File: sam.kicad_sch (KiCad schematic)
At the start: 46 parts, among them IC1 4164, IC15 MC6883, IC16 74LS244N, IC2 4164, IC3 4164, IC31 74LS02N, IC33 74AHCT138N, IC36 74LS132, IC37 GAL, IC4 4164, IC5 4164, IC6 4164, IC7 4164, IC8 4164, U1 74HCT138

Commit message: move to samx4
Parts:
- removed C11, C37: 4.7uF, Capacitor_THT:CP_Radial_D5.0mm_P2.50mm, symbol Device:C_Polarized_Small
- removed C14, C15, C16, C17, C18, C19, C20, C21: 0.1uF, Capacitor_THT:C_Disc_D4.3mm_W1.9mm_P5.00mm, symbol Device:C_Small
- removed C40: 22pF, Capacitor_THT:C_Disc_D3.0mm_W2.0mm_P2.50mm, symbol Device:C_Small
- removed C41: 33pF, Capacitor_THT:C_Disc_D3.0mm_W2.0mm_P2.50mm, symbol Device:C_Small
- removed IC1, IC2, IC3, IC4, IC5, IC6, IC7, IC8: 4164, Package_DIP:DIP-16_W7.62mm, symbol Memory_RAM_Siemens:HYB4116
- removed IC15: MC6883, Package_DIP:DIP-40_W15.24mm, symbol Memory_Controller_Motorola:MC6883
- removed unit 2 of IC36
- removed unit 4 of IC36
- removed unit 3 of IC36
- removed unit 1 of IC36
- removed IC37: GAL, Package_DIP:DIP-24_W7.62mm, symbol vdg:GAL22V10
- removed JP5: Z8hi/low, Jumper:SolderJumper-3_P1.3mm_Open_Pad1.0x1.5mm, symbol Jumper:Jumper_3_Bridged12
- removed R12, R20, R21, R22, R23, R24, R25, R26, R27, R28, R66: 22R, Resistor_THT:R_Axial_DIN0207_L6.3mm_D2.5mm_P2.54mm_Vertical, symbol Device:R_Small
- removed R37: 1K5, Resistor_THT:R_Axial_DIN0207_L6.3mm_D2.5mm_P10.16mm_Horizontal, symbol Device:R_Small
- removed XL2: 14.31818MHz, Crystal:Crystal_HC49-U_Horizontal, symbol Device:Crystal_Small
- added C11, C13, C14, C15, C16, C7: 100n, Capacitor_SMD:C_0603_1608Metric, symbol Device:C
- added C3, C5: 0.1uF, Capacitor_THT:C_Disc_D4.3mm_W1.9mm_P5.00mm, symbol Device:C_Small
- added C6: 4.7uF, Capacitor_THT:CP_Radial_D5.0mm_P2.50mm, symbol Device:C_Polarized_Small
- added C8: 1u, Capacitor_SMD:C_0805_2012Metric, symbol Device:C
- added C9: 2u2, Capacitor_SMD:C_0603_1608Metric, symbol Device:C
- added IC11: 74LS244N, Package_DIP:DIP-20_W7.62mm, symbol 74xx:74LS244
- added J4: JTAG, Connector_PinHeader_2.54mm:PinHeader_1x06_P2.54mm_Vertical, symbol Connector_Generic:Conn_01x06
- added R10, R11, R17, R18, R2, R3, R4, R6, R7, R8, R9: 22R, Resistor_THT:R_Axial_DIN0207_L6.3mm_D2.5mm_P2.54mm_Vertical, symbol Device:R_Small
- added R5: 100R, Resistor_THT:R_Axial_DIN0207_L6.3mm_D2.5mm_P2.54mm_Vertical, symbol Device:R_Small
- added U1, U2: ~, symbol Motorola PIA:AS6C1008
- added U3: XC95144XL-TQ100, Package_QFP:TQFP-100_14x14mm_P0.5mm, symbol CPLD_Xilinx:XC95144XL-TQ100
- added U4: TPS7A2433DBVR, Package_TO_SOT_SMD:SOT-23-5, symbol Regulator_Linear:TPS7A0533PDBV
- added X1: 14.31818MHz, Oscillator:Oscillator_SMD_ECS_2520MV-xxx-xx-4Pin_2.5x2.0mm, symbol Oscillator:ECS-2520MV-xxx-xx
- C12: footprint Capacitor_THT:C_Rect_L7.0mm_W2.5mm_P5.00mm -> Capacitor_SMD:C_0603_1608Metric; JLCPCB BOM (none) -> 0; LCSC Part (none) -> C149620
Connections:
- net +5V: now also C3.2, C5.2, C6.1, C8.1, IC11.20 (VCC), U1.6 (CE2), U1.8 (Vcc), U2.8 (Vcc), U4.1 (IN), U4.3 (EN); no longer C12.1
- net A0: now also U1.20 (A0), U2.20 (A0), U3.80 (P80)
- net A1: now also U1.19 (A1), U2.19 (A1), U3.78 (P78)
- net A10: now also U1.31 (A10), U2.31 (A10), U3.19 (P19)
- net A11: now also U1.1 (A11), U2.1 (A11), U3.20 (P20)
- net A12: now also U1.12 (A12), U2.12 (A12), U3.12 (P12)
- net A13: now also U1.4 (A13), U2.4 (A13), U3.14 (P14)
- net A14: now also U1.11 (A14), U2.11 (A14), U3.9 (P9)
- net A15: now also U1.7 (A15), U2.7 (A15), U3.8 (P8)
- net A2: now also U1.18 (A2), U2.18 (A2), U3.76 (P76)
- net A3: now also U1.17 (A3), U2.17 (A3), U3.63 (P63)
- net A4: now also U1.16 (A4), U2.16 (A4), U3.58 (P58)
- net A5: now also U1.15 (A5), U2.15 (A5), U3.59 (P59)
- net A6: now also U1.14 (A6), U2.14 (A6), U3.60 (P60)
- net A7: now also U1.13 (A7), U2.13 (A7), U3.61 (P61)
- net A8: now also U1.3 (A8), U2.3 (A8), U3.17 (P17)
- net A9: now also U1.2 (A9), U2.2 (A9), U3.18 (P18)
- net D0: now also IC11.15 (I2b)
- net D1: now also IC11.13 (I1b)
- net D2: now also IC11.4 (I1a)
- net D3: now also IC11.2 (I0a)
- net D4: now also IC11.17 (I3b)
- net D5: now also IC11.6 (I2a)
- net D6: now also IC11.8 (I3a)
- net D7: now also IC11.11 (I0b)
- net DA0: now also U3.22 (I/O/GCK1)
- net DO0: now also IC11.5 (O2b), U1.21 (DQ0), U2.21 (DQ0)
- net DO1: now also IC11.7 (O1b), U1.22 (DQ1), U2.22 (DQ1)
- net DO2: now also IC11.16 (O1a), U1.23 (DQ2), U2.23 (DQ2)
- net DO3: now also IC11.18 (O0a), U1.25 (DQ3), U2.25 (DQ3)
- net DO4: now also IC11.3 (O3b), U1.26 (DQ4), U2.26 (DQ4)
- net DO5: now also IC11.14 (O2a), U1.27 (DQ5), U2.27 (DQ5)
- net DO6: now also IC11.12 (O3a), U1.28 (DQ6), U2.28 (DQ6)
- net DO7: now also IC11.9 (O0b), U1.29 (DQ7), U2.29 (DQ7)
- net E: now also U3.91 (P91)
- net GND: now also C11.2, C13.2, C14.2, C15.2, C16.2, C3.1, C5.1, C6.2, C7.2, C8.2, C9.2, IC11.10 (GND), J4.2 (Pin_2), U1.24 (Vss), U2.24 (Vss), U2.30 (~{CE}), U3.10 (P10), U3.100 (GND), U3.11 (P11), U3.13 (P13), U3.15 (P15), U3.16 (P16), U3.2 (I/O/GTS4), U3.21 (GND), U3.24 (P24), U3.25 (P25), U3.27 (I/O/GCK3), U3.28 (P28), U3.29 (P29), U3.3 (I/O/GTS1), U3.30 (P30), U3.31 (GND), U3.32 (P32), U3.33 (P33), U3.34 (P34), U3.35 (P35), U3.36 (P36), U3.37 (P37), U3.39 (P39), U3.4 (I/O/GTS2), U3.40 (P40), U3.41 (P41), U3.42 (P42), U3.43 (P43), U3.44 (GND), U3.50 (P50), U3.52 (P52), U3.54 (P54), U3.55 (P55), U3.6 (P6), U3.62 (GND), U3.64 (P64), U3.66 (P66), U3.69 (GND), U3.7 (P7), U3.73 (P73), U3.75 (GND), U3.81 (P81), U3.82 (P82), U3.84 (GND), U3.86 (P86), U3.90 (P90), U3.92 (P92), U3.93 (P93), U3.95 (P95), U3.96 (P96), U4.2 (GND), X1.2 (GND)
- net Q: now also U3.97 (P97)
- net R/~{W}: now also IC31.5, IC31.6, U1.5 (~{WE}), U2.5 (~{WE}), U3.87 (P87)
- net S0: now also U3.79 (P79)
- net S1: now also U3.77 (P77)
- net S2: now also U3.74 (P74)
- net VCLK: now also R5.1, U3.99 (I/O/GSR)
- net Z0: now also R6.1
- net Z1: now also R7.1
- net Z2: now also R8.1
- net Z3: now also R9.1
- net Z4: now also R10.1
- net Z5: now also R11.1; no longer R19.1
- net Z6: now also R17.1
- net Z7: now also R18.1
- net Z8: now also R19.1
- net ~{CAS}: now also R3.1, U1.32 (~{OE}), U2.32 (~{OE})
- net ~{NHS}: now also U3.46 (P46)
- net ~{WE}: now also R4.1
- net at R19.2: now also U3.49 (P49)
- net at IC31.4: now also IC11.1 (OEa), IC11.19 (OEb)
- new net: R4.2, U3.53 (P53)
- new net: R18.2, U3.56 (P56)
- new net: R6.2, U3.85 (P85)
- new net: R9.2, U3.65 (P65)
- new net: R5.2, U3.1 (I/O/GTS3)
- new net: R2.2, U3.71 (P71)
- new net: R10.2, U3.67 (P67)
- new net: R3.2, U3.68 (P68)
- new net: R11.2, U3.70 (P70)
- new net: R17.2, U3.72 (P72)
- new net: R7.2, U3.89 (P89)
- new net: R8.2, U3.94 (P94)
- new net +3V3: C11.1, C12.1, C13.1, C14.1, C15.1, C16.1, C7.1, C9.1, J4.1 (Pin_1), U3.26 (VCCIO), U3.38 (VCCIO), U3.5 (VCCINT), U3.51 (VCCIO), U3.57 (VCCINT), U3.88 (VCCIO), U3.98 (VCCINT), U4.5 (OUT), X1.4 (VDD)
- new net A16: U1.10 (A16), U2.10 (A16)
- new net A17: U1.30 (~{CE}), U2.6 (CE2)
- new net OSC: U3.23 (I/O/GCK2), X1.3 (OUT)
- new net TCK: J4.3 (Pin_3), U3.48 (TCK)
- new net TDI0: J4.5 (Pin_5), U3.45 (TDI)
- new net TDI1: J4.4 (Pin_4), U3.83 (TDO)
- new net TMS: J4.6 (Pin_6), U3.47 (TMS)
- no-connect marks 10 -> 2
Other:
- company: (none) -> Dragon Data
- title: (none) -> Dragon 32 CPU UK PAL
- moved on the sheet: C10, IC16, IC31A, IC31B, IC31D, IC33, IC36E, JP1, R39, U1

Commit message: rework board
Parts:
- removed C10: 100n, Capacitor_THT:C_Rect_L7.0mm_W2.5mm_P5.00mm, symbol Device:C
- removed IC36: 74LS132, Package_DIP:DIP-14_W7.62mm, symbol 74xx:74LS132
- added R12, R20, R21, R22, R23, R24, R25, R26, R27: 22R, Resistor_SMD:R_0805_2012Metric_Pad1.20x1.40mm_HandSolder, symbol Device:R_Small
- C11, C12, C13, C14, C15, C16, C7, C9: footprint Capacitor_SMD:C_0603_1608Metric -> Capacitor_SMD:C_0805_2012Metric_Pad1.18x1.45mm_HandSolder
- C3, C5: footprint Capacitor_THT:C_Disc_D4.3mm_W1.9mm_P5.00mm -> Capacitor_SMD:C_0805_2012Metric_Pad1.18x1.45mm_HandSolder
- C6: footprint Capacitor_THT:CP_Radial_D5.0mm_P2.50mm -> Capacitor_Tantalum_SMD:CP_EIA-3216-18_Kemet-A_Pad1.58x1.35mm_HandSolder
- C8: footprint Capacitor_SMD:C_0805_2012Metric -> Capacitor_SMD:C_0805_2012Metric_Pad1.18x1.45mm_HandSolder
- IC11, IC16: value 74LS244N -> 74ACT244N; footprint Package_DIP:DIP-20_W7.62mm -> Package_SO:SOIC-20W_7.5x12.8mm_P1.27mm; DigiKey 296-1653-5-ND -> 74ACT244SCXCT-ND
- IC31: value 74LS02N -> 74ACT02; footprint Package_DIP:DIP-14_W7.62mm -> Package_SO:SOIC-14_3.9x8.7mm_P1.27mm; DigiKey 296-1627-5-ND -> MC74ACT02DR2GOSCT-ND
- IC33: value 74AHCT138N -> 74ACT138N; footprint Package_DIP:DIP-16_W7.62mm -> Package_SO:SOIC-20W_7.5x12.8mm_P1.27mm; DigiKey 296-1639-5-ND -> 74ACT138SCXCT-ND
- R10, R11, R17, R18, R19, R2, R3, R39, R4, R5, R6, R7, R8, R9: footprint Resistor_THT:R_Axial_DIN0207_L6.3mm_D2.5mm_P2.54mm_Vertical -> Resistor_SMD:R_0805_2012Metric_Pad1.20x1.40mm_HandSolder
- U1: value 74HCT138 -> 74ACT138; footprint Package_DIP:DIP-16_W7.62mm -> Package_SO:SOIC-20W_7.5x12.8mm_P1.27mm; DigiKey (none) -> 74ACT138SCXCT-ND
- U1: value ~ -> AS6C1008-TIN; footprint (none) -> Package_SO:TSOP-I-32_18.4x8mm_P0.5mm; DigiKey (none) -> 1450-1020-ND
- U2: value ~ -> AS6C1008-55TIN; footprint (none) -> Package_SO:TSOP-I-32_18.4x8mm_P0.5mm; DigiKey (none) -> 1450-1020-ND
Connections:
- net A0: no longer U1.20 (A0), U2.20 (A0)
- net A1: no longer U1.19 (A1), U2.19 (A1)
- net A10: no longer U1.31 (A10), U2.31 (A10)
- net A11: no longer U1.1 (A11), U2.1 (A11)
- net A12: no longer U1.12 (A12), U2.12 (A12)
- net A13: no longer U1.4 (A13), U2.4 (A13)
- net A14: no longer U1.11 (A14), U2.11 (A14)
- net A15: no longer U1.7 (A15), U2.7 (A15)
- net A2: no longer U1.18 (A2), U2.18 (A2)
- net A3: no longer U1.17 (A3), U2.17 (A3)
- net A4: no longer U1.16 (A4), U2.16 (A4)
- net A5: no longer U1.15 (A5), U2.15 (A5)
- net A6: no longer U1.14 (A6), U2.14 (A6)
- net A7: no longer U1.13 (A7), U2.13 (A7)
- net A8: no longer U1.3 (A8), U2.3 (A8)
- net A9: no longer U1.2 (A9), U2.2 (A9)
- net GND: no longer U3.35 (P35), U3.36 (P36), U3.37 (P37), U3.39 (P39), U3.40 (P40), U3.41 (P41), U3.42 (P42), U3.43 (P43), U3.81 (P81)
- net Z0: now also U1.20 (A0), U2.20 (A0)
- net Z1: now also U1.19 (A1), U2.19 (A1)
- net Z2: now also U1.18 (A2), U2.18 (A2)
- net Z3: now also U1.17 (A3), U2.17 (A3)
- net Z4: now also U1.16 (A4), U2.16 (A4)
- net Z5: now also U1.15 (A5), U2.15 (A5)
- net Z6: now also U1.14 (A6), U2.14 (A6)
- net Z7: now also U1.13 (A7), U2.13 (A7)
- net Z8: now also U1.3 (A8), U2.3 (A8)
- net A16 renamed Z16
- net Z16: now also R26.1
- net A17 renamed Z17
- net Z17: now also R27.1
- new net: R23.2, U3.40 (P40)
- new net: R20.2, U3.36 (P36)
- new net: R22.2, U3.39 (P39)
- new net: R12.2, U3.35 (P35)
- new net: R27.2, U3.81 (P81)
- new net: R26.2, U3.43 (P43)
- new net: R21.2, U3.37 (P37)
- new net: R24.2, U3.41 (P41)
- new net: R25.2, U3.42 (P42)
- new net Z10: R20.1, U1.31 (A10), U2.31 (A10)
- new net Z11: R21.1, U1.1 (A11), U2.1 (A11)
- new net Z12: R22.1, U1.12 (A12), U2.12 (A12)
- new net Z13: R23.1, U1.4 (A13), U2.4 (A13)
- new net Z14: R24.1, U1.11 (A14), U2.11 (A14)
- new net Z15: R25.1, U1.7 (A15), U2.7 (A15)
- new net Z9: R12.1, U1.2 (A9), U2.2 (A9)
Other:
- moved on the sheet: C11, C12, C13, C14, C15, C16, C3, C5, C6, C7, C8, C9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

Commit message: serial wiring
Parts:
- IC33, U1: footprint Package_SO:SOIC-20W_7.5x12.8mm_P1.27mm -> Package_SO:SOIC-16W_7.5x10.3mm_P1.27mm
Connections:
- net D0: now also IC16.14 (O2a); no longer IC16.5 (O2b)
- net D1: now also IC16.16 (O1a); no longer IC16.7 (O1b)
- net D2: now also IC16.7 (O1b); no longer IC16.16 (O1a)
- net D3: now also IC16.9 (O0b); no longer IC16.18 (O0a)
- net D4: now also IC16.12 (O3a); no longer IC16.3 (O3b)
- net D5: now also IC16.5 (O2b); no longer IC16.14 (O2a)
- net D6: now also IC16.3 (O3b); no longer IC16.12 (O3a)
- net D7: now also IC16.18 (O0a); no longer IC16.9 (O0b)
- net DO0: now also IC16.6 (I2a); no longer IC16.15 (I2b)
- net DO1: now also IC16.4 (I1a); no longer IC16.13 (I1b)
- net DO2: now also IC16.13 (I1b); no longer IC16.4 (I1a)
- net DO3: now also IC16.11 (I0b); no longer IC16.2 (I0a)
- net DO4: now also IC16.8 (I3a); no longer IC16.17 (I3b)
- net DO5: now also IC16.15 (I2b); no longer IC16.6 (I2a)
- net DO6: now also IC16.17 (I3b); no longer IC16.8 (I3a)
- net DO7: now also IC16.2 (I0a); no longer IC16.11 (I0b)
- net ~{RAS0}: now also R2.1

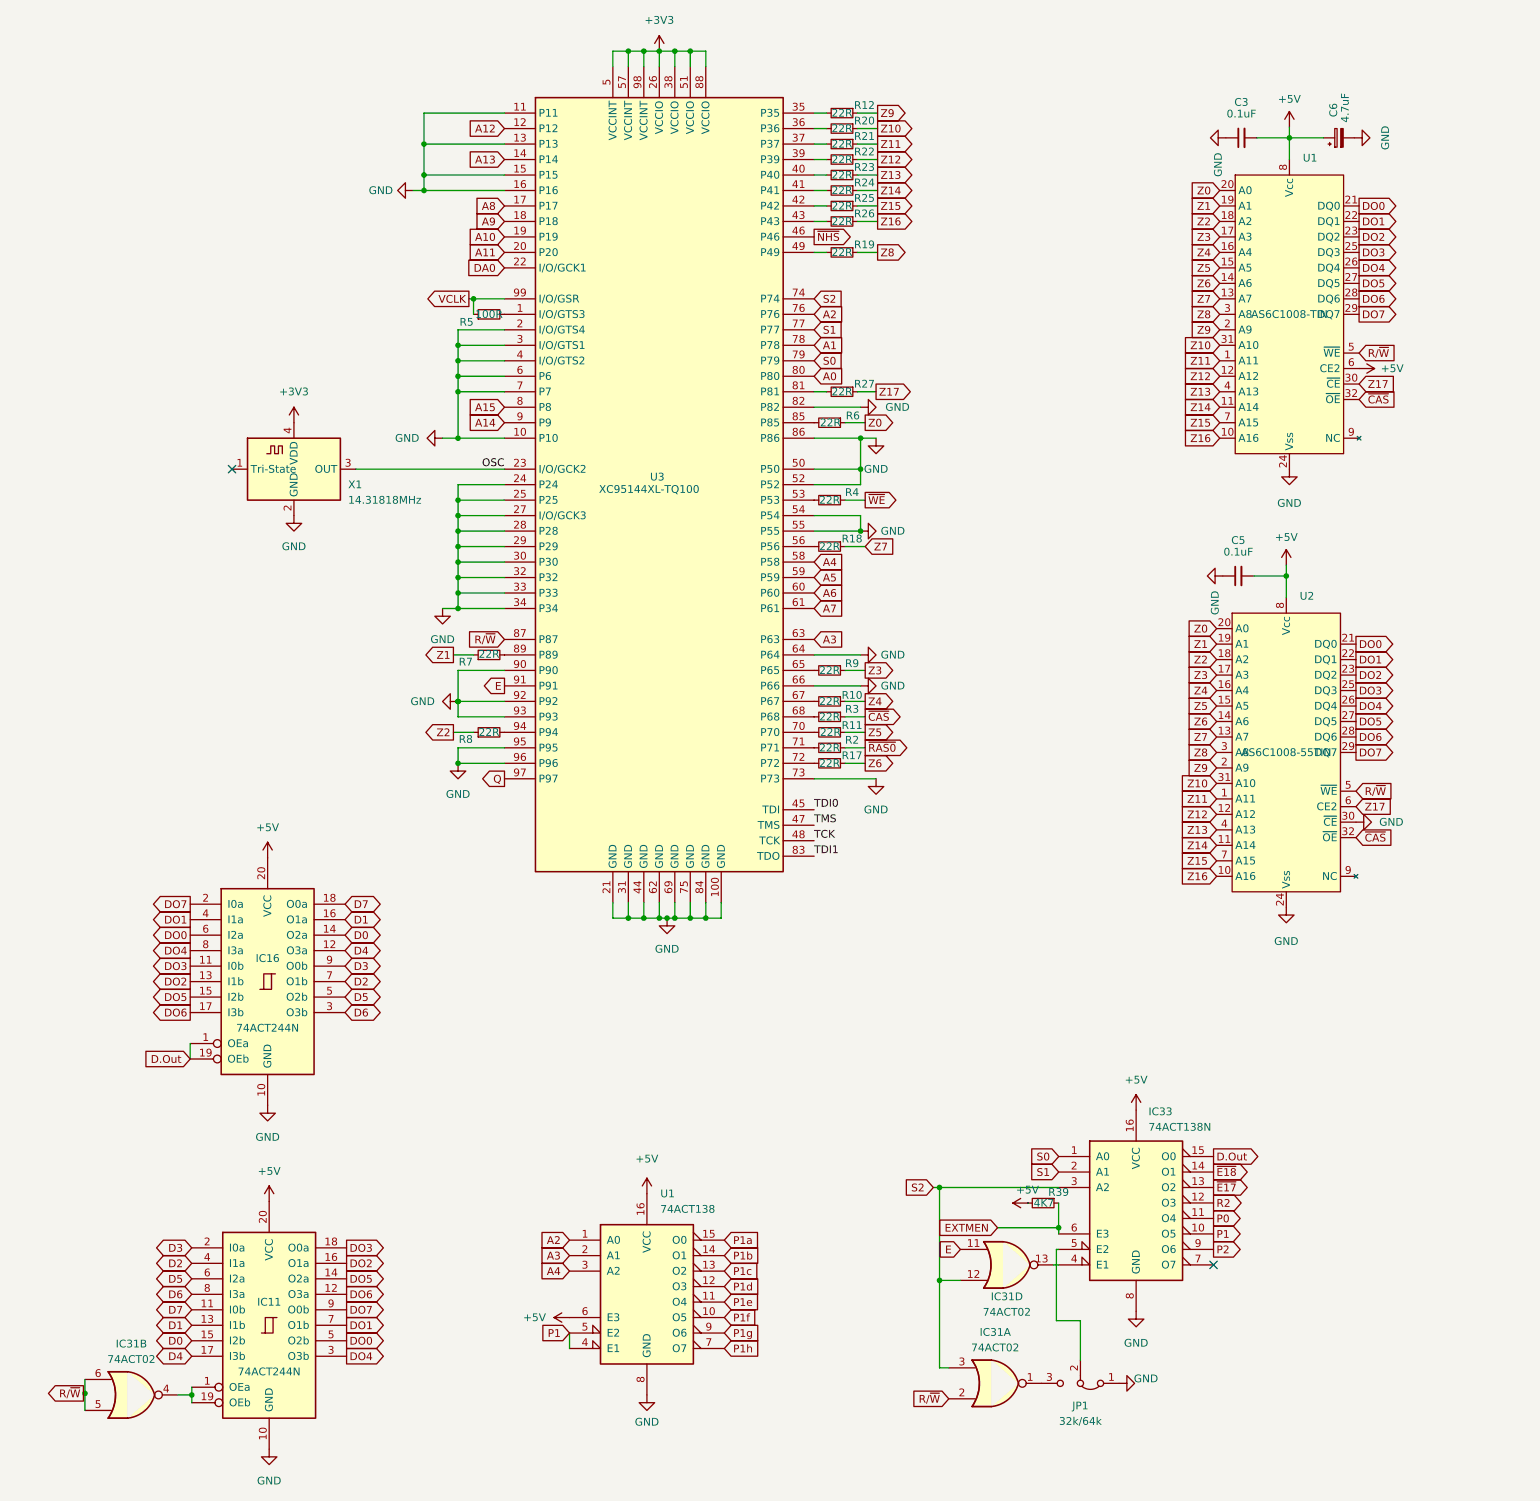
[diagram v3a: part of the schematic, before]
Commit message: fix OE timing on SRAM
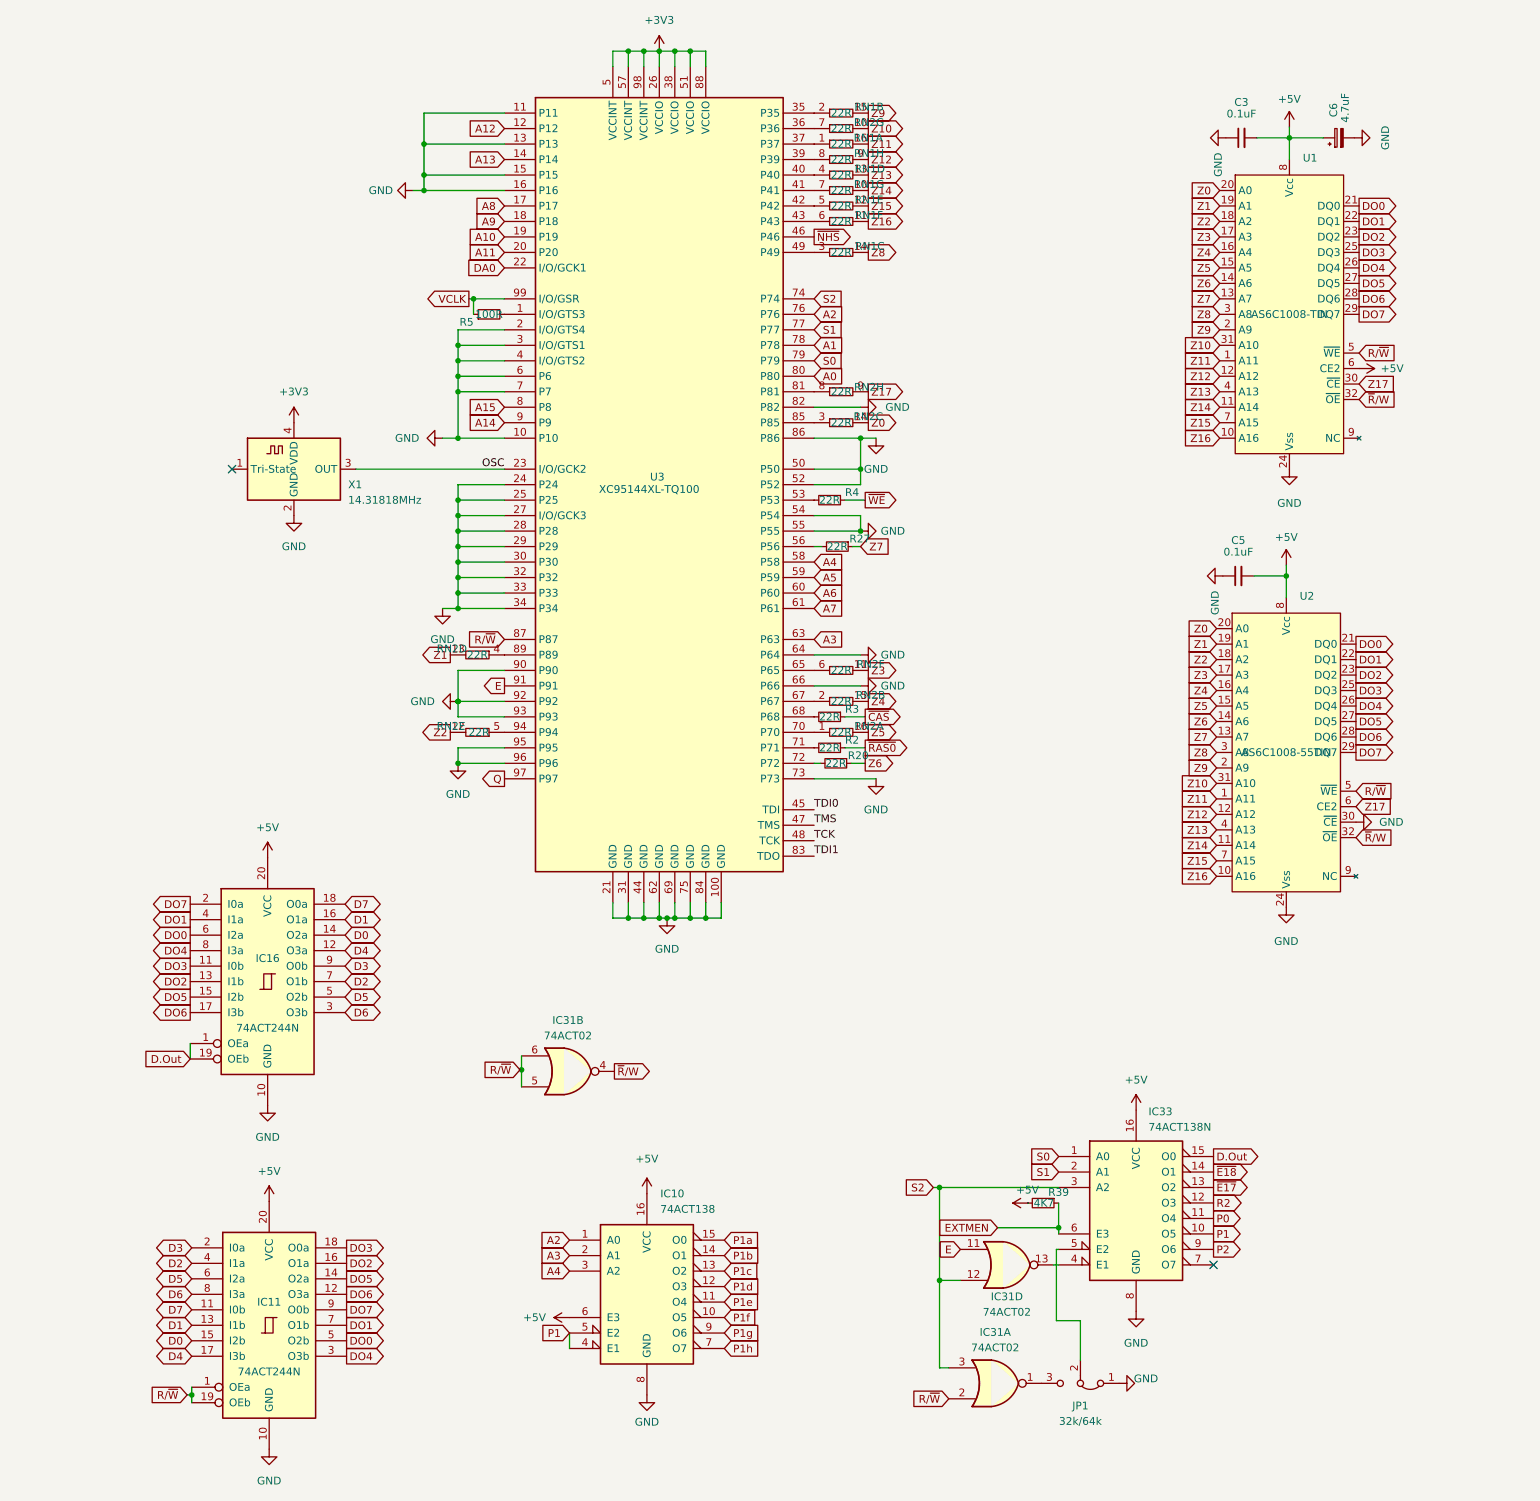
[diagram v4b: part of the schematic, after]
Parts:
- removed R10, R11, R12, R17, R18, R19, R21, R22, R23, R24, R25, R26, R6, R7, R8, R9: 22R, Resistor_SMD:R_0805_2012Metric_Pad1.20x1.40mm_HandSolder, symbol Device:R_Small
- added RN1, RN2: 22R, Package_SO:SOIC-16_3.9x9.9mm_P1.27mm, symbol Motorola PIA:R_Pack_Split
- renumbered U1 to IC10
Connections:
- net R/~{W}: now also IC11.1 (OEa), IC11.19 (OEb)
- net Z0: now also RN2.14
- net Z1: now also RN2.13
- net Z10: now also RN2.10; no longer R20.1
- net Z11: now also RN1.16
- net Z12: now also RN1.9
- net Z13: now also RN1.13
- net Z14: now also RN1.10
- net Z15: now also RN1.12
- net Z16: now also RN1.11
- net Z17: now also RN2.9; no longer R27.1
- net Z2: now also RN2.12
- net Z3: now also RN2.11
- net Z4: now also RN2.15
- net Z5: now also RN2.16
- net Z6: now also R20.1
- net Z7: now also R27.1
- net Z8: now also RN1.14
- net Z9: now also RN1.15
- net ~{CAS}: no longer U1.32 (~{OE}), U2.32 (~{OE})
- net at U3.40 (P40): now also RN1.4
- net at U3.56 (P56): now also R27.2
- net at R20.2: now also U3.72 (P72); no longer U3.36 (P36)
- net at U3.39 (P39): now also RN1.8
- net at U3.35 (P35): now also RN1.2
- net at U3.85 (P85): now also RN2.3
- net at U3.49 (P49): now also RN1.3
- net at U3.81 (P81): now also RN2.8; no longer R27.2
- net at U3.65 (P65): now also RN2.6
- net at U3.43 (P43): now also RN1.6
- net at U3.37 (P37): now also RN1.1
- net at U3.41 (P41): now also RN1.7
- net at U3.42 (P42): now also RN1.5
- net at U3.67 (P67): now also RN2.2
- net at U3.70 (P70): now also RN2.1
- net at U3.89 (P89): now also RN2.4
- net at U3.94 (P94): now also RN2.5
- new net: RN2.7, U3.36 (P36)
- new net ~{R}/W: IC31.4, U1.32 (~{OE}), U2.32 (~{OE})
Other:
- moved on the sheet: IC31B, R20, R27

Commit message: move -5v
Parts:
- X1: RS (none) -> https://uk.rs-online.com/web/p/crystal-oscillators/1721882
